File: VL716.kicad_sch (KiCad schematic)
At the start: 25 parts, among them U1 VL716-Q4, Y1 25Mhz Crystal

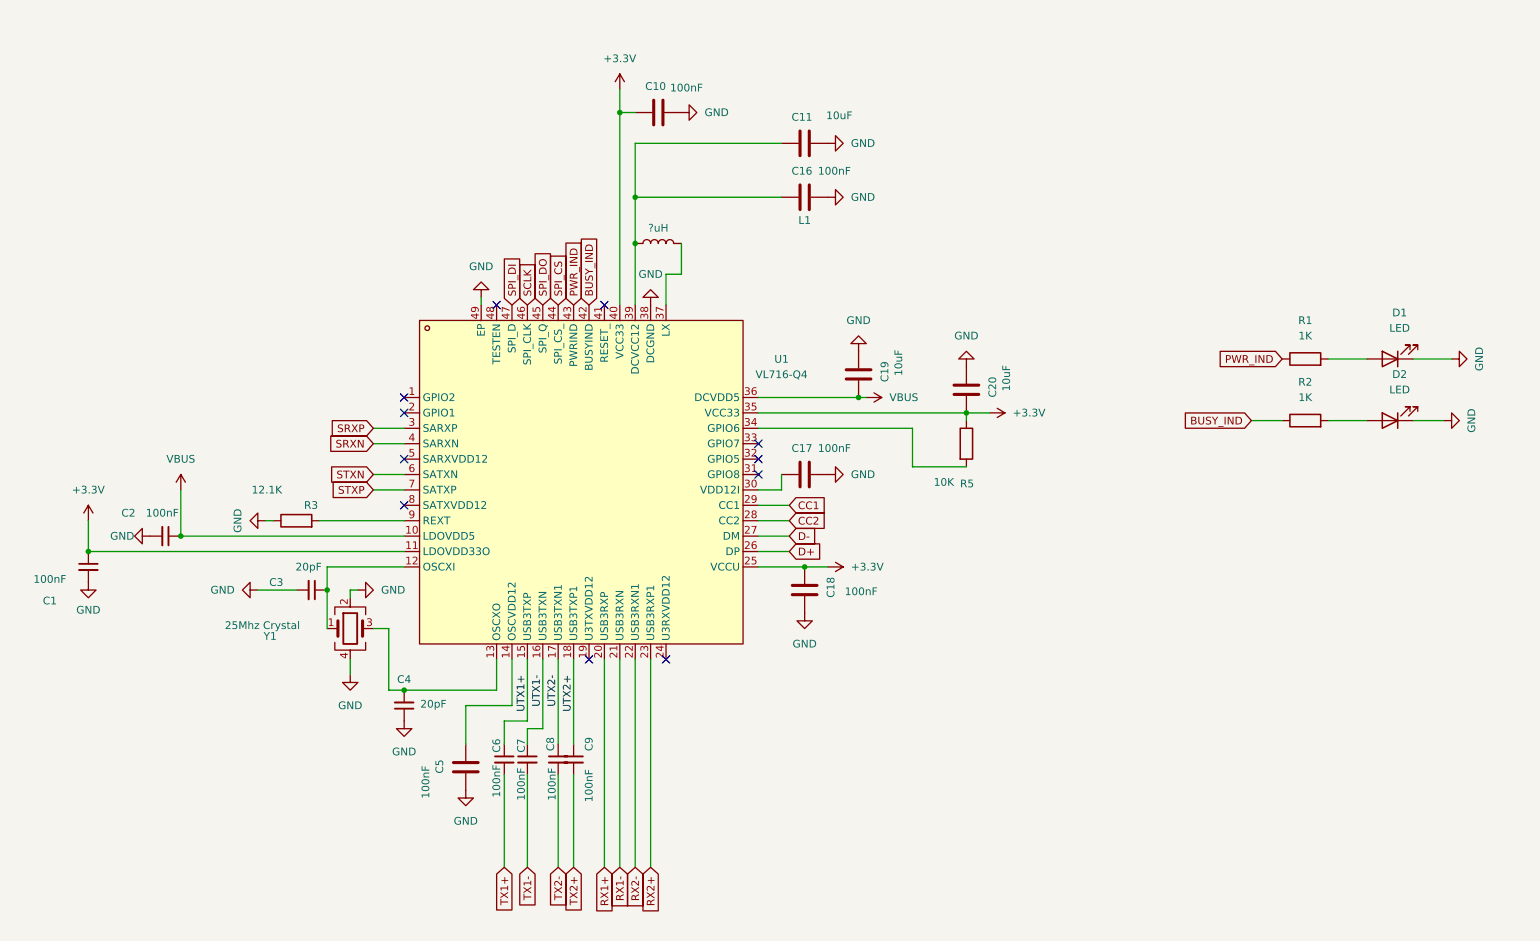
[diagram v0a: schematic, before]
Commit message: Fixed layout
Fixed traces length
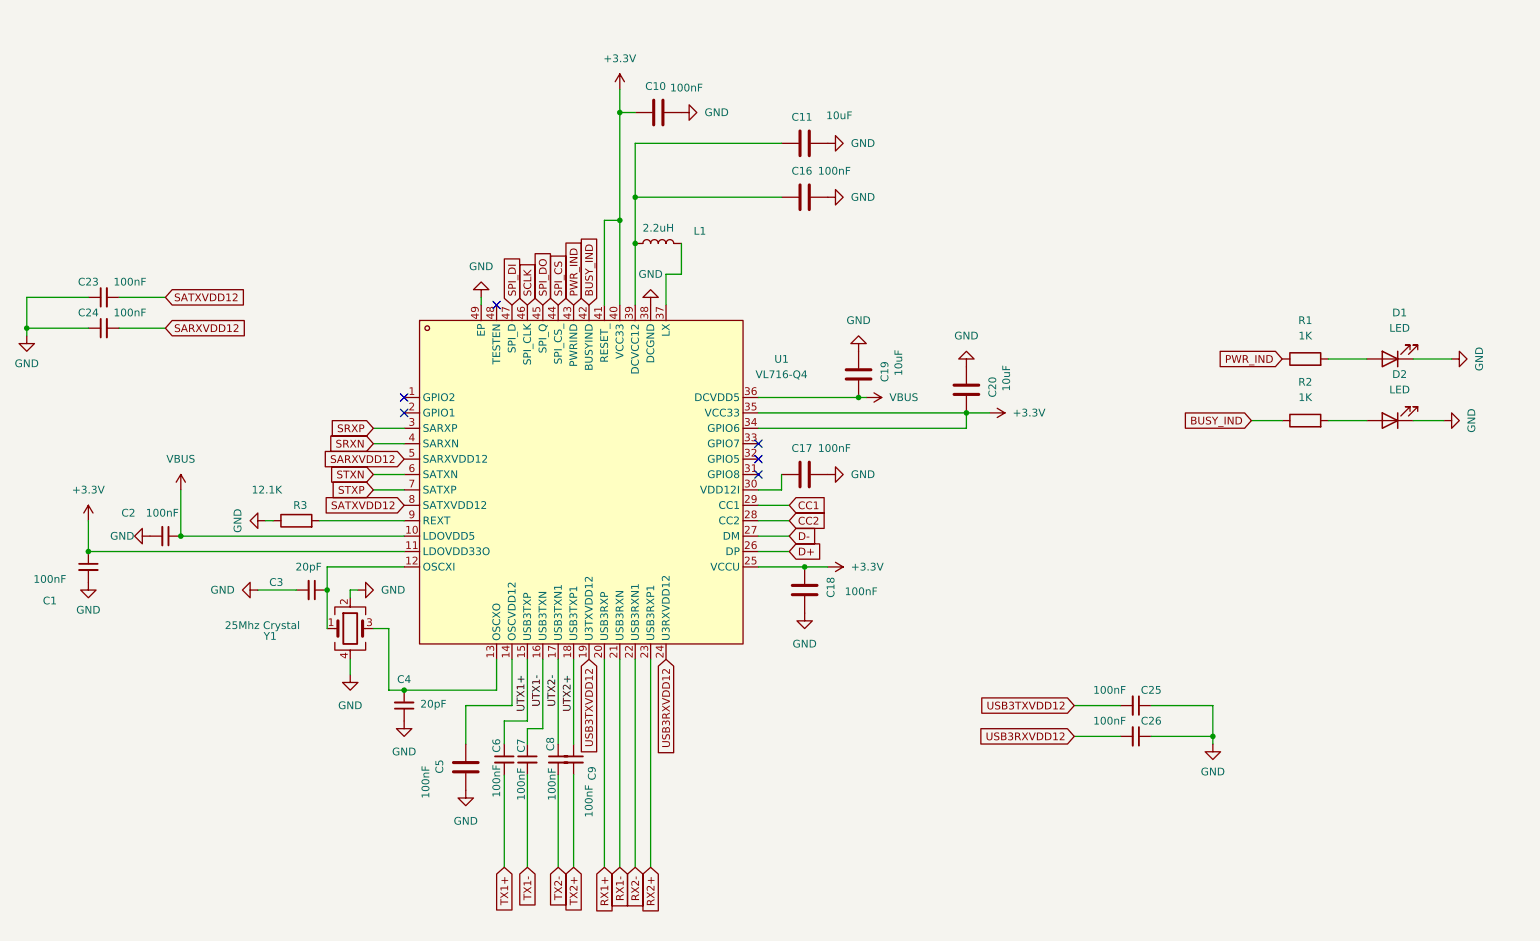
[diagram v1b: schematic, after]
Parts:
- removed R5: 10K, Resistor_SMD:R_0402_1005Metric, symbol Device:R
- added C23, C24, C25, C26: 100nF, Capacitor_SMD:C_0402_1005Metric, symbol Device:C_Small
- L1: value ?uH -> 2.2uH; footprint Inductor_SMD:L_Cenker_CKCS5040 -> Inductor_SMD:L_Cenker_CKCS4030
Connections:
- net +3.3V: now also U1.34 (GPIO6), U1.41 (RESET_)
- net GND: now also C23.1, C24.1, C25.1, C26.1
- net USB3TXVDD12: now reaches U1.19 (U3TXVDD12)
- net USB3TXVDD12: now also C25.2
- net USB3RXVDD12: now reaches U1.24 (U3RXVDD12)
- net USB3RXVDD12: now also C26.2
- net SARXVDD12: now reaches U1.5 (SARXVDD12)
- net SARXVDD12: now also C24.2
- net SATXVDD12: now reaches U1.8 (SATXVDD12)
- net SATXVDD12: now also C23.2
- no-connect marks 11 -> 6

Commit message: .
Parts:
- removed C23, C24: 100nF, Capacitor_SMD:C_0402_1005Metric, symbol Device:C_Small
- added C29, C30: 100nF, Capacitor_SMD:C_0402_1005Metric, symbol Device:C_Small
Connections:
- net SARXVDD12 is gone; now on net +1V2: U1.5 (SARXVDD12)
- net SATXVDD12 is gone; now on net +1V2: U1.8 (SATXVDD12)
- net USB3RXVDD12 is gone; now on net +1V2: C26.2, U1.24 (U3RXVDD12)
- net USB3TXVDD12 is gone; now on net +1V2: C25.2, U1.19 (U3TXVDD12)
- net GND: now also C29.2, C30.2
- net +1V2: now reaches C11.1, C16.1, L1.1, U1.39 (DCVCC12)
- net +1V2: now also C17.1, C5.2, U1.14 (OSCVDD12), U1.30 (VDD12I), C29.1, C30.1
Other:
- moved on the sheet: C1, C10, C11, C16, C17, C18, C19, C2, C20, C25, C26, C3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
